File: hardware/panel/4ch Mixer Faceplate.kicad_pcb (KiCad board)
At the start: 2 copper layers, 30.5 x 128.5 mm, 15 parts

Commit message: Swap + and - output positions on the panel; trim pot ring at the edge
Board: J5 (non-inverting, +) is on the right and J6 (inverting, -) on the left,
after the designator and net swap. Panel: + to the right of the J5 hole, -
to the left of the J6 hole. Pot outer rings are cut at the panel edge.
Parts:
- moved JH5 13.9 mm to (122.0, 145.0)
- moved JH6 13.9 mm to (108.1, 145.0)
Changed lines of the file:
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@@
 	)
 	(gr_text "+"
-		(at 101.527 145.0 0)
+		(at 128.55 145.0 0)
 		(layer "F.SilkS")
 		(effects
@@
 	)
 	(gr_text "-"
-		(at 128.55 145.0 0)
+		(at 101.527 145.0 0)
 		(layer "F.SilkS")
 		(effects
@@
 	(gr_arc
 		(start 121.5091 48.4058)
-		(mid 131.25 56.5186)
+		(mid 126.5012 49.0498)
+		(end 130.19 52.4745)
+		(stroke
+			(width 0.2)
+			(type default)
+		)
+		(layer "F.SilkS")
+	)
+	(gr_arc
+		(start 130.19 60.5655)
+		(mid 126.5024 63.9896)
 		(end 121.5118 64.6347)
 		(stroke
@@
 	(gr_arc
 		(start 121.5091 72.4058)
-		(mid 131.25 80.5186)
+		(mid 126.5012 73.0498)
+		(end 130.19 76.4745)
+		(stroke
+			(width 0.2)
+			(type default)
+		)
+		(layer "F.SilkS")
+	)
+	(gr_arc
+		(start 130.19 84.5655)
+		(mid 126.5024 87.9896)
 		(end 121.5118 88.6347)
 		(stroke
@@
 	(gr_arc
 		(start 121.5091 96.4058)
-		(mid 131.25 104.5186)
+		(mid 126.5012 97.0498)
+		(end 130.19 100.4745)
+		(stroke
+			(width 0.2)
+			(type default)
+		)
+		(layer "F.SilkS")
+	)
+	(gr_arc
+		(start 130.19 108.5655)
+		(mid 126.5024 111.9896)
 		(end 121.5118 112.6347)
 		(stroke
@@
 	(gr_arc
 		(start 121.5091 120.4058)
-		(mid 131.25 128.5186)
+		(mid 126.5012 121.0498)
+		(end 130.19 124.4745)
+		(stroke
+			(width 0.2)
+			(type default)
+		)
+		(layer "F.SilkS")
+	)
+	(gr_arc
+		(start 130.19 132.5655)
+		(mid 126.5024 135.9896)
 		(end 121.5118 136.6347)
 		(stroke
@@
 	(footprint "Panel:Jack_6mm"
 		(layer "F.Cu")
-		(at 108.077 145.0)
+		(at 122.0 145.0)
 		(attr board_only exclude_from_pos_files exclude_from_bom)
 		(property "Reference" "JH5"
@@
 	)
 	(gr_circle
-		(center 108.077 145.0)
-		(end 110.527 145.0)
+		(center 122.0 145.0)
+		(end 124.45 145.0)
 		(stroke
 			(width 5.0)
@@
 	(footprint "Panel:Jack_6mm"
 		(layer "F.Cu")
-		(at 122.0 145.0)
+		(at 108.077 145.0)
 		(attr board_only exclude_from_pos_files exclude_from_bom)
 		(property "Reference" "JH6"
@@
 	)
 	(gr_circle
-		(center 122.0 145.0)
-		(end 124.45 145.0)
+		(center 108.077 145.0)
+		(end 110.527 145.0)
 		(stroke
 			(width 5.0)

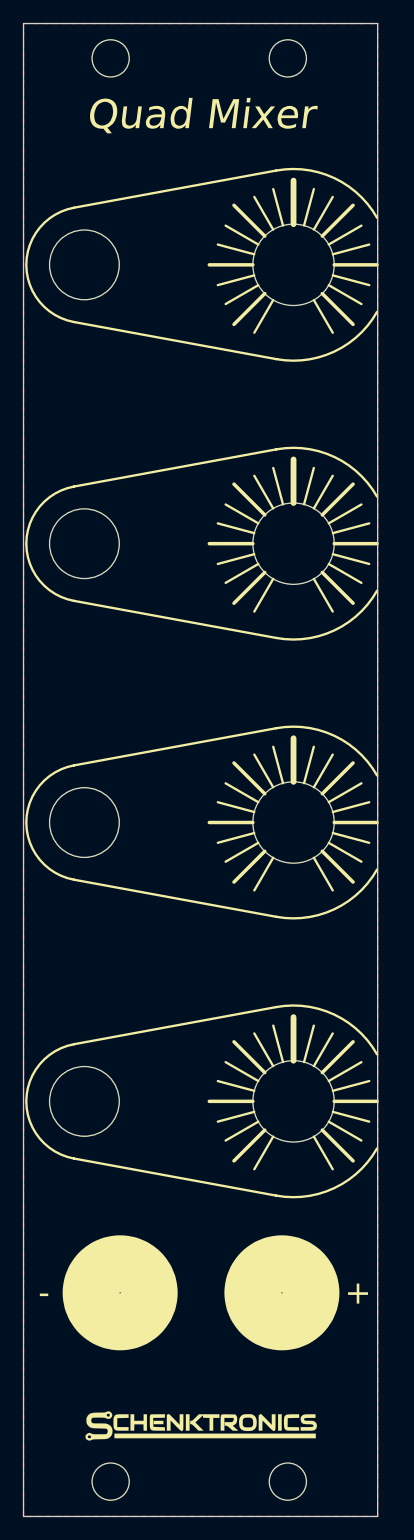
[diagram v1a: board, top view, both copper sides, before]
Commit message: Faceplate: trim to true 30mm (6HP at 5.0mm/HP), matching the main PCB
Was 30.48mm (5.08mm/HP, the official Eurorack spec), inconsistent with
the rest of the lineup and with the main PCB, which was already 30mm.
Trimmed 0.24mm off each edge, keeping the same centerline (X=115.0) as
the main board. Checked every hole, jack, pot and the wordmark against
the new edges first — nearest is the '+' text at 1.45mm clear, nothing
clips.
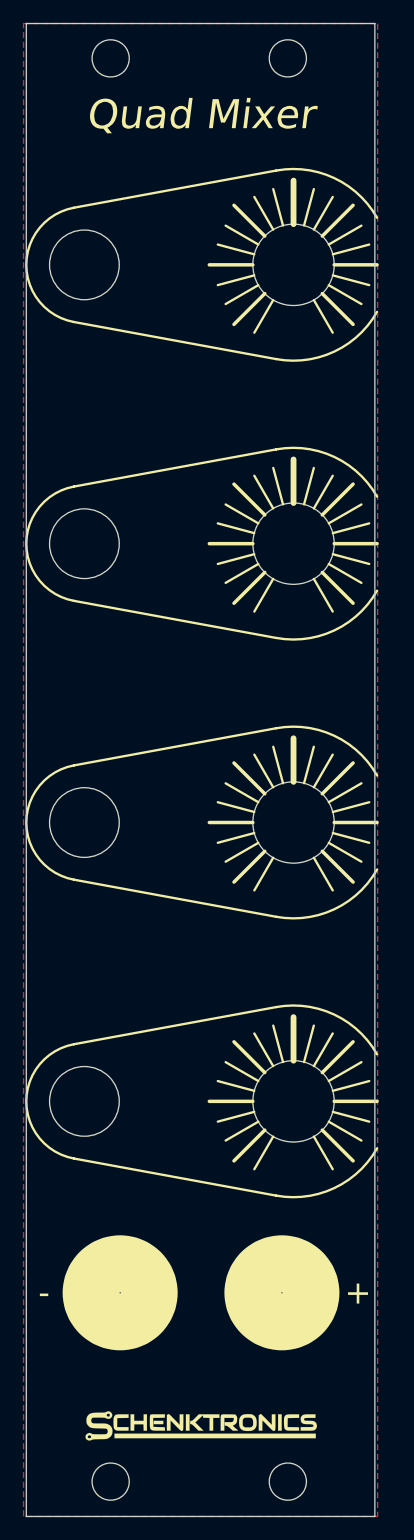
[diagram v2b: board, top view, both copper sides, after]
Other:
- board size 30.5 x 128.5 mm -> 30 x 128.5 mm
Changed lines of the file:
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@@
 	(net 1 "GND")
 	(gr_line
-		(start 99.76 35.75)
-		(end 130.24 35.75)
+		(start 100.0 35.75)
+		(end 130.0 35.75)
 		(stroke
 			(width 0.05)
@@
 	)
 	(gr_line
-		(start 130.24 35.75)
-		(end 130.24 164.25)
+		(start 130.0 35.75)
+		(end 130.0 164.25)
 		(stroke
 			(width 0.05)
@@
 	)
 	(gr_line
-		(start 130.24 164.25)
-		(end 99.76 164.25)
+		(start 130.0 164.25)
+		(end 100.0 164.25)
 		(stroke
 			(width 0.05)
@@
 	)
 	(gr_line
-		(start 99.76 164.25)
-		(end 99.76 35.75)
+		(start 100.0 164.25)
+		(end 100.0 35.75)
 		(stroke
 			(width 0.05)

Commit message: Faceplate: squeezed wordmark footer, Orbitron text
Replaces the lower-left S-mark with the 2mm-squeezed full wordmark
(_NTSFootprints:SchentronicsLogoSqueeze2mm), centered in the gap right
of the bottom screw hole (0.92mm margin each side). Adds ST-04, vertical,
centered in the left gap, anchored to the wordmark's bottom. Header and
part number switched from italic KiCad stroke font to upright Orbitron.

Note: this file carries other pending local changes from before this
edit, not just the faceplate update above.
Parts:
- removed H2, H4: , Panel:MountingHole_3.2mm
- removed LOGO: , SchentronicsLogo
- added G***: LOGO, _NTSFootprints:SchentronicsLogoSqueeze2mm, F.Cu at (120.1, 161.2)
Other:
- board text added: "ST-04"

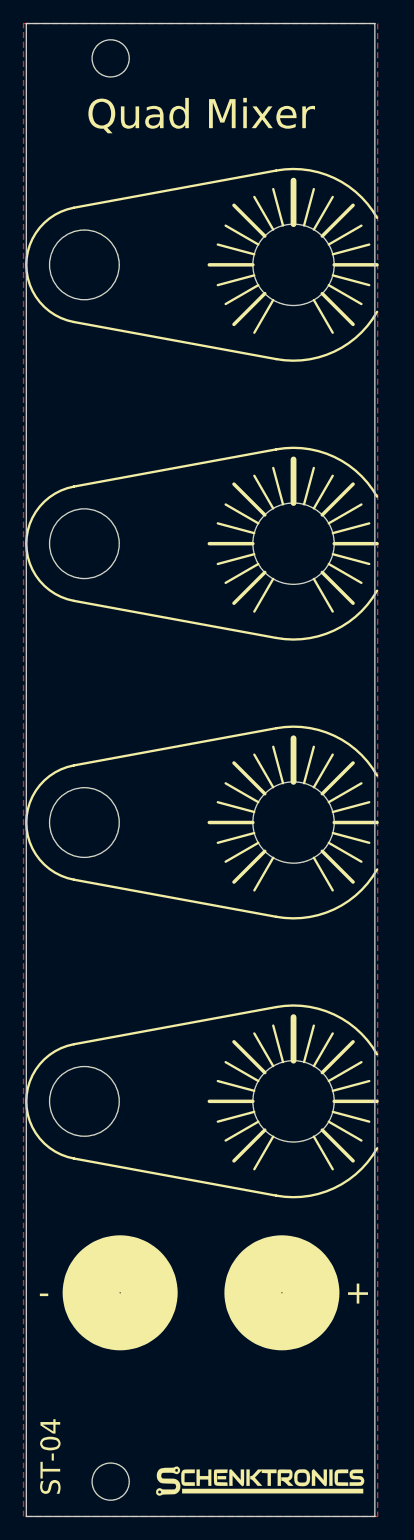
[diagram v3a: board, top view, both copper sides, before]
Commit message: Faceplate: align mounting-hole X-offset to 7.5mm, re-anchor wordmark/ST-04
Both rack-screw holes move from 7.26mm off the left edge to exactly
7.5mm, matching the Attenuverter and the two 3 HP boards -- this board's
holes were 0.24mm further left than the Attenuverter's, a real mismatch,
not rounding. Wordmark and ST-04 shift by the same 0.12mm to stay
centered off the new hole position.
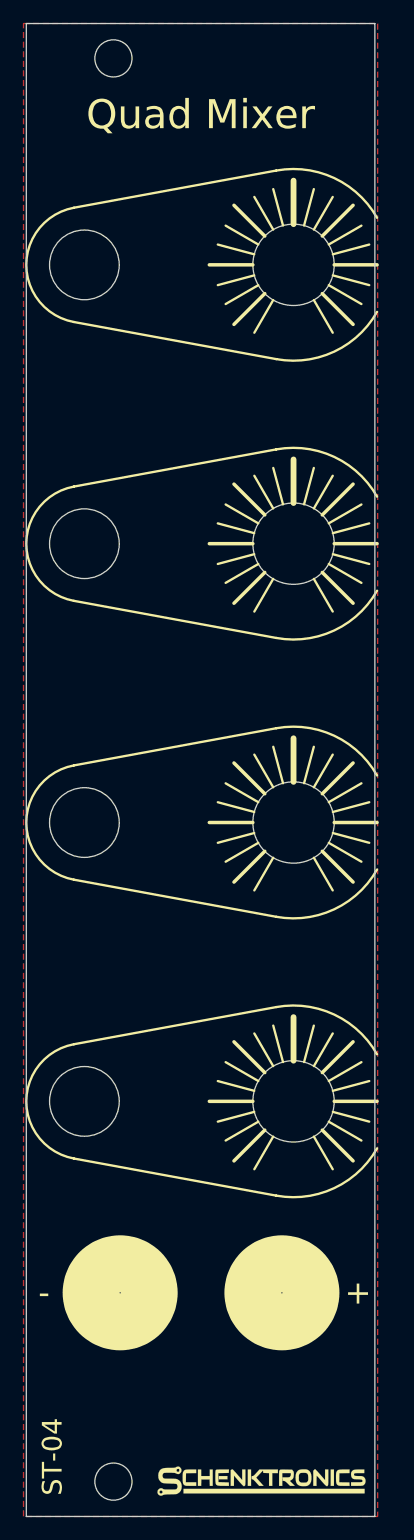
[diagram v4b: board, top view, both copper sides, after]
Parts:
- moved H1 0.24 mm to (107.5, 38.8)
- moved H3 0.24 mm to (107.5, 161.2)
- moved G*** 0.12 mm to (120.2, 161.2)
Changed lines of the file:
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@@
 	(footprint "Panel:MountingHole_3.2mm"
 		(layer "F.Cu")
-		(at 107.26 38.75)
+		(at 107.5 38.75)
 		(attr board_only exclude_from_pos_files exclude_from_bom)
 		(property "Reference" "H1"
@@
 	(footprint "Panel:MountingHole_3.2mm"
 		(layer "F.Cu")
-		(at 107.26 161.25)
+		(at 107.5 161.25)
 		(attr board_only exclude_from_pos_files exclude_from_bom)
 		(property "Reference" "H3"
@@
 	)
 	(gr_text "ST-04"
-		(at 102.1300 162.4597 90)
+		(at 102.2500 162.4597 90)
 		(layer "F.SilkS")
 		(effects
@@
 		(footprint "_NTSFootprints:SchentronicsLogoSqueeze2mm"
 		(layer "F.Cu")
-		(at 120.0867 161.2500)
+		(at 120.2067 161.2500)
 		(property "Reference" "G***" (at 0 0 0) (layer "F.SilkS") (hide yes) (effects (font (size 1.524 1.524) (thickness 0.3))))
 		(property "Value" "LOGO" (at 0.75 0 0) (layer "F.SilkS") (hide yes) (effects (font (size 1.524 1.524) (thickness 0.3))))
